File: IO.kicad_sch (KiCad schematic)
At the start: 11 parts, among them J6 JST_SH_1x6_SM06B-SRSS-TB-LF-SN, J7 JST_SH_1x6_SM06B-SRSS-TB-LF-SN, U13 TPD4E05U06QDQARQ1, U14 TPD4E05U06QDQARQ1

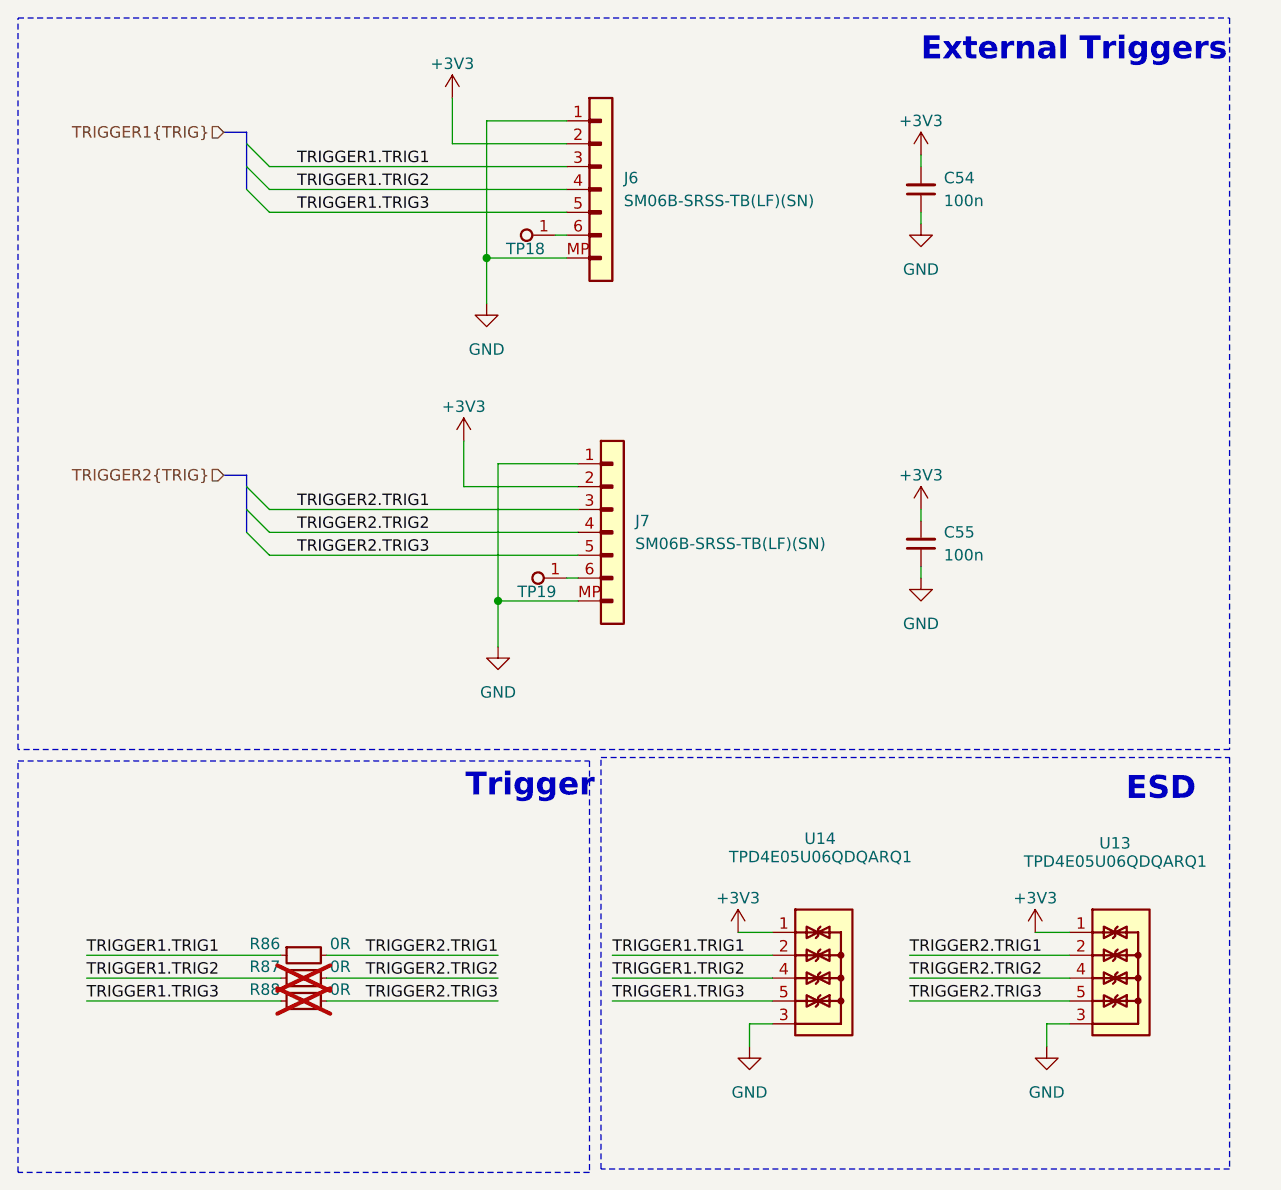
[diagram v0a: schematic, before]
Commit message: [#71986] Add 4th trigger I/O
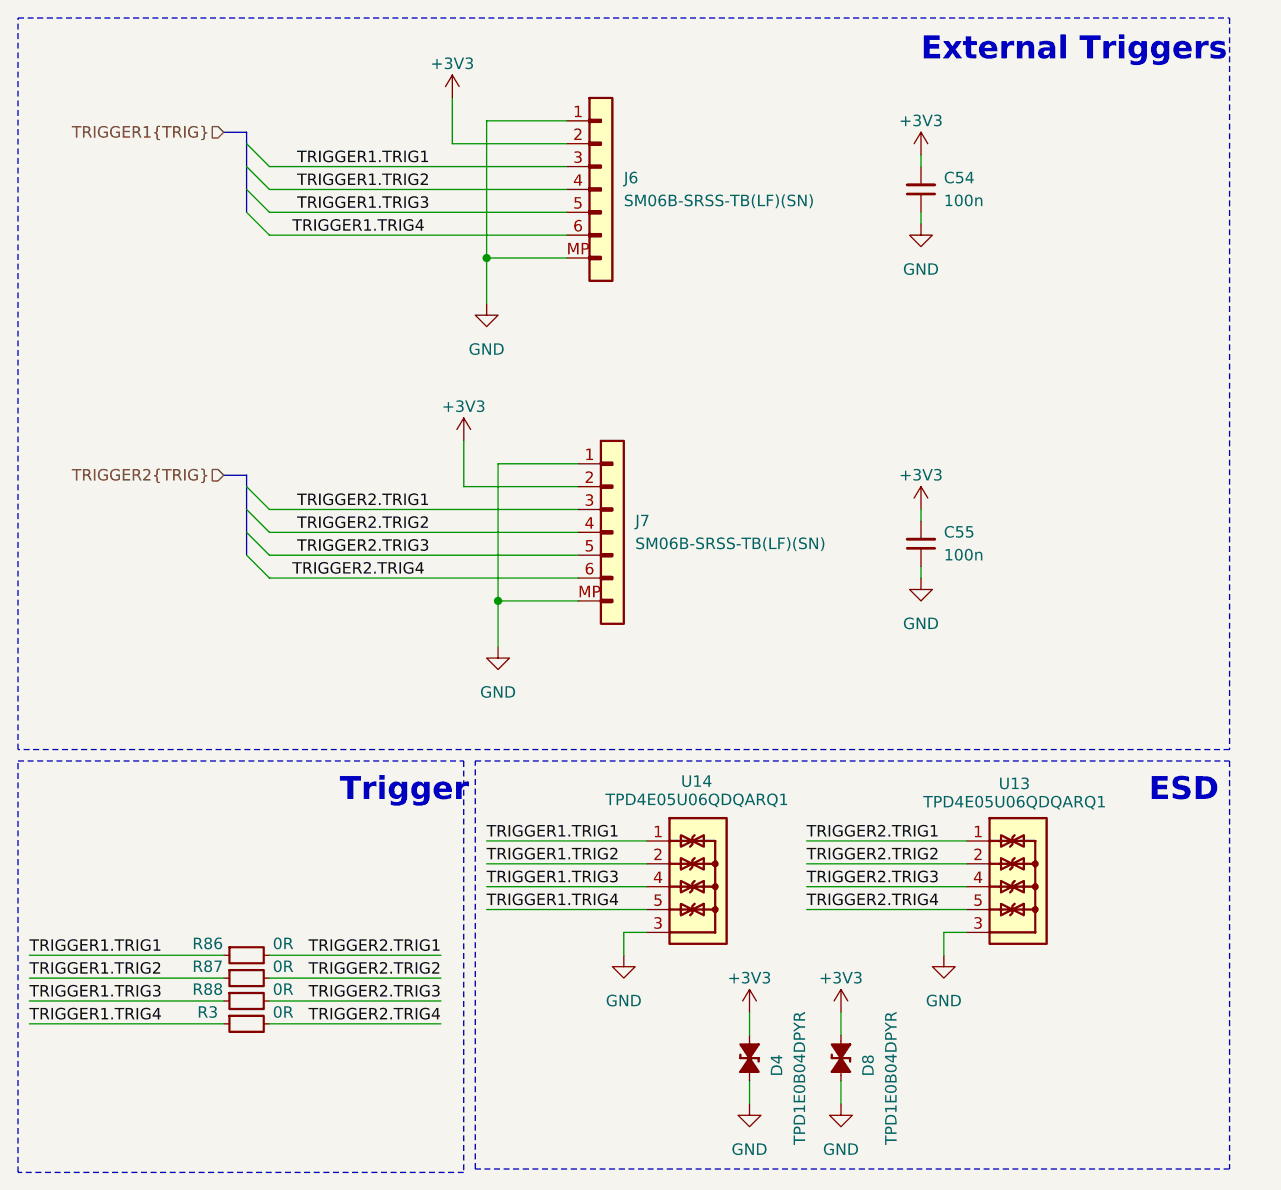
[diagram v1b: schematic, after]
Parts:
- removed TP18, TP19: TP_0.75mm_SMD, antmicro-footprints:TP_SMD_0.75mm, symbol antmicroTestPoints:TP_0.75mm_SMD
- added D4, D8: TPD1E0B04_XDFN-2, antmicro-footprints:XDFN-2_1x0.60mm, symbol antmicroTVSDiodes:TPD1E0B04_XDFN-2
- added R3: R_0R_0402, antmicro-footprints:R_0402_1005Metric, symbol antmicroResistors0402:R_0R_0402
- R87, R88: now fitted
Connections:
- net +3V3: now also D4.2 (A), D8.2 (A); no longer U13.1, U13.10, U14.1, U14.10
- net GND: now also D4.1 (C), D8.1 (C)
- net TRIGGER1.TRIG1: now also U14.1, U14.10; no longer U14.2, U14.9
- net TRIGGER1.TRIG2: now also U14.2, U14.9; no longer U14.4, U14.7
- net TRIGGER1.TRIG3: now also U14.4, U14.7; no longer U14.5, U14.6
- net TRIGGER2.TRIG1: now also U13.1, U13.10; no longer U13.2, U13.9
- net TRIGGER2.TRIG2: now also U13.2, U13.9; no longer U13.4, U13.7
- net TRIGGER2.TRIG3: now also U13.4, U13.7; no longer U13.5, U13.6
- net TRIGGER2.TRIG4: now reaches J7.6
- net TRIGGER2.TRIG4: now also U13.5, U13.6, R3.2
- net TRIGGER1.TRIG4: now reaches J6.6
- net TRIGGER1.TRIG4: now also U14.5, U14.6, R3.1
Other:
- moved on the sheet: R86, U13, U14

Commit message: [#71249] Update project name
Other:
- title: Audio Latency Processing Board -> Audio controller board
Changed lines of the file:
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@@
 	(paper "A3")
 	(title_block
-		(title "Audio Latency Processing Board")
+		(title "Audio controller board")
 		(date "2025-01-20")
 		(rev "1.2.0")
@@
 	(label "TRIGGER2.TRIG4"
 		(at 167.64 146.05 0)
+		(fields_autoplaced yes)
 		(effects
 			(font
@@
 	(label "TRIGGER1.TRIG4"
 		(at 167.64 107.95 0)
+		(fields_autoplaced yes)
 		(effects
 			(font
@@
 		)
 		(instances
-			(project "audio-latency-processing-board"
+			(project "audio-controller-board"
 				(path "/7fb12ebf-f685-4412-b638-445b1bf344bc/1277d361-8469-440e-97d3-29bbfd6c9b73"
 					(reference "#PWR0132")
@@
 		)
 		(instances
-			(project "audio-latency-processing-board"
+			(project "audio-controller-board"
 				(path "/7fb12ebf-f685-4412-b638-445b1bf344bc/1277d361-8469-440e-97d3-29bbfd6c9b73"
 					(reference "#PWR035")
@@
 		)
 		(instances
-			(project "audio-latency-processing-board"
+			(project "audio-controller-board"
 				(path "/7fb12ebf-f685-4412-b638-445b1bf344bc/1277d361-8469-440e-97d3-29bbfd6c9b73"
 					(reference "#PWR04")
@@
 		)
 		(instances
-			(project "audio-latency-processing-board"
+			(project "audio-controller-board"
 				(path "/7fb12ebf-f685-4412-b638-445b1bf344bc/1277d361-8469-440e-97d3-29bbfd6c9b73"
 					(reference "R88")
@@
 		)
 		(instances
-			(project "audio-latency-processing-board"
+			(project "audio-controller-board"
 				(path "/7fb12ebf-f685-4412-b638-445b1bf344bc/1277d361-8469-440e-97d3-29bbfd6c9b73"
 					(reference "#PWR0134")
@@
 		)
 		(instances
-			(project "audio-latency-processing-board"
+			(project "audio-controller-board"
 				(path "/7fb12ebf-f685-4412-b638-445b1bf344bc/1277d361-8469-440e-97d3-29bbfd6c9b73"
 					(reference "#PWR0125")
@@
 		)
 		(instances
-			(project "audio-latency-processing-board"
+			(project "audio-controller-board"
 				(path "/7fb12ebf-f685-4412-b638-445b1bf344bc/1277d361-8469-440e-97d3-29bbfd6c9b73"
 					(reference "U14")
@@
 		)
 		(instances
-			(project "audio-latency-processing-board"
+			(project "audio-controller-board"
 				(path "/7fb12ebf-f685-4412-b638-445b1bf344bc/1277d361-8469-440e-97d3-29bbfd6c9b73"
 					(reference "J7")
@@
 		)
 		(instances
-			(project "audio-latency-processing-board"
+			(project "audio-controller-board"
 				(path "/7fb12ebf-f685-4412-b638-445b1bf344bc/1277d361-8469-440e-97d3-29bbfd6c9b73"
 					(reference "#PWR0126")
@@
 		)
 		(instances
-			(project "audio-latency-processing-board"
+			(project "audio-controller-board"
 				(path "/7fb12ebf-f685-4412-b638-445b1bf344bc/1277d361-8469-440e-97d3-29bbfd6c9b73"
 					(reference "R3")
@@
 		)
 		(instances
-			(project "audio-latency-processing-board"
+			(project "audio-controller-board"
 				(path "/7fb12ebf-f685-4412-b638-445b1bf344bc/1277d361-8469-440e-97d3-29bbfd6c9b73"
 					(reference "D8")
@@
 		)
 		(instances
-			(project "audio-latency-processing-board"
+			(project "audio-controller-board"
 				(path "/7fb12ebf-f685-4412-b638-445b1bf344bc/1277d361-8469-440e-97d3-29bbfd6c9b73"
 					(reference "#PWR0151")
@@
 		)
 		(instances
-			(project "audio-latency-processing-board"
+			(project "audio-controller-board"
 				(path "/7fb12ebf-f685-4412-b638-445b1bf344bc/1277d361-8469-440e-97d3-29bbfd6c9b73"
 					(reference "#PWR0124")
@@
 		)
 		(instances
-			(project "audio-latency-processing-board"
+			(project "audio-controller-board"
 				(path "/7fb12ebf-f685-4412-b638-445b1bf344bc/1277d361-8469-440e-97d3-29bbfd6c9b73"
 					(reference "R87")
@@
 		)
 		(instances
-			(project "audio-latency-processing-board"
+			(project "audio-controller-board"
 				(path "/7fb12ebf-f685-4412-b638-445b1bf344bc/1277d361-8469-440e-97d3-29bbfd6c9b73"
 					(reference "#PWR0135")
@@
 		)
 		(instances
-			(project "audio-latency-processing-board"
+			(project "audio-controller-board"
 				(path "/7fb12ebf-f685-4412-b638-445b1bf344bc/1277d361-8469-440e-97d3-29bbfd6c9b73"
 					(reference "U13")
@@
 		)
 		(instances
-			(project "audio-latency-processing-board"
+			(project "audio-controller-board"
 				(path "/7fb12ebf-f685-4412-b638-445b1bf344bc/1277d361-8469-440e-97d3-29bbfd6c9b73"
 					(reference "#PWR0133")
@@
 		)
 		(instances
-			(project "audio-latency-processing-board"
+			(project "audio-controller-board"
 				(path "/7fb12ebf-f685-4412-b638-445b1bf344bc/1277d361-8469-440e-97d3-29bbfd6c9b73"
 					(reference "D4")
@@
 		)
 		(instances
-			(project "audio-latency-processing-board"
+			(project "audio-controller-board"
 				(path "/7fb12ebf-f685-4412-b638-445b1bf344bc/1277d361-8469-440e-97d3-29bbfd6c9b73"
 					(reference "#PWR0152")
@@
 		)
 		(instances
-			(project "audio-latency-processing-board"
+			(project "audio-controller-board"
 				(path "/7fb12ebf-f685-4412-b638-445b1bf344bc/1277d361-8469-440e-97d3-29bbfd6c9b73"
 					(reference "#PWR0150")
@@
 		)
 		(instances
-			(project "audio-latency-processing-board"
+			(project "audio-controller-board"
 				(path "/7fb12ebf-f685-4412-b638-445b1bf344bc/1277d361-8469-440e-97d3-29bbfd6c9b73"
 					(reference "C55")
@@
 		)
 		(instances
-			(project "audio-latency-processing-board"
+			(project "audio-controller-board"
 				(path "/7fb12ebf-f685-4412-b638-445b1bf344bc/1277d361-8469-440e-97d3-29bbfd6c9b73"
 					(reference "#PWR02")
